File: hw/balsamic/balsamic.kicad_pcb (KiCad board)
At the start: 2 copper layers, 24 x 39 mm, 125 parts, among them J1 Conn_01x24, J2 USB_C_Receptacle, SW1 SW_Push, U1 ISP1807-LR-RS, U2 BMI160, U3 K210, U4 MAX77658AANX+, U5 GD25LQ, U6 MAX811LEUS-T, U7 SiP32431DR3, Y1 Crystal_GND24

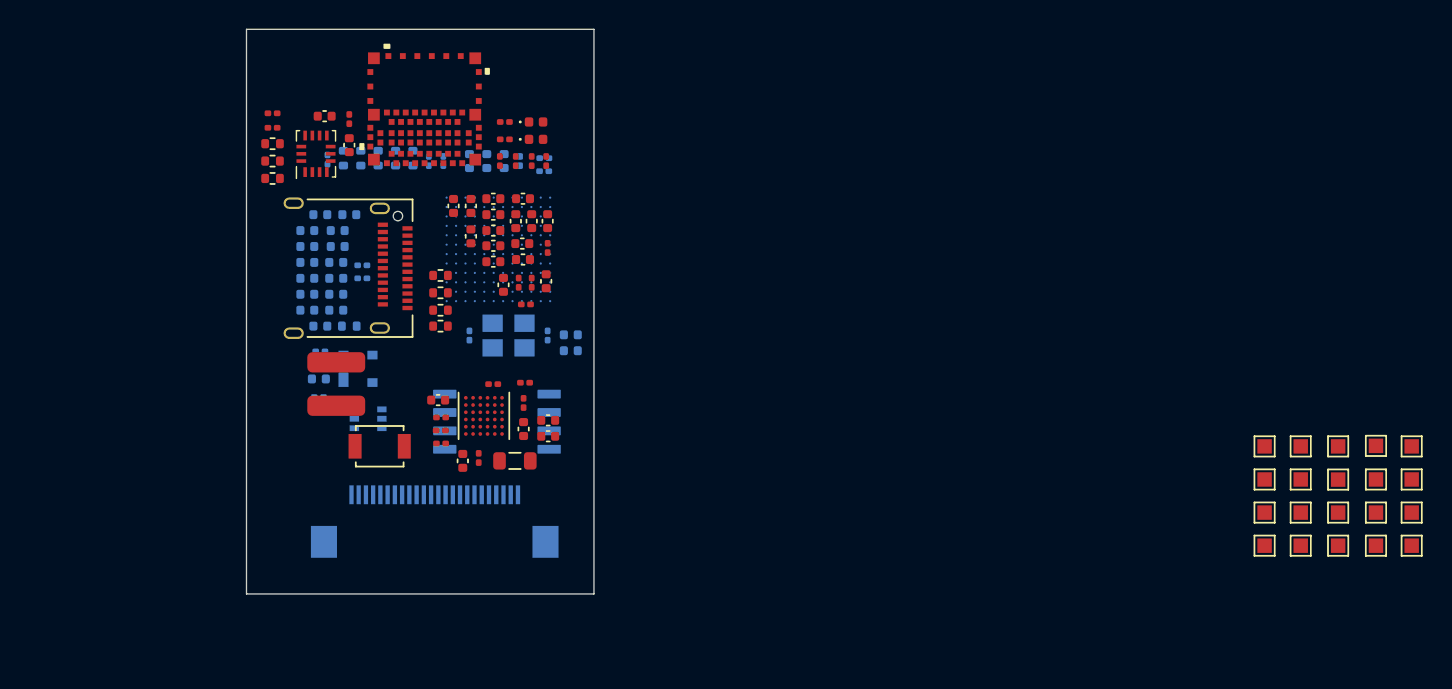
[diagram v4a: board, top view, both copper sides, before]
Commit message: Reduced spacing between ICs
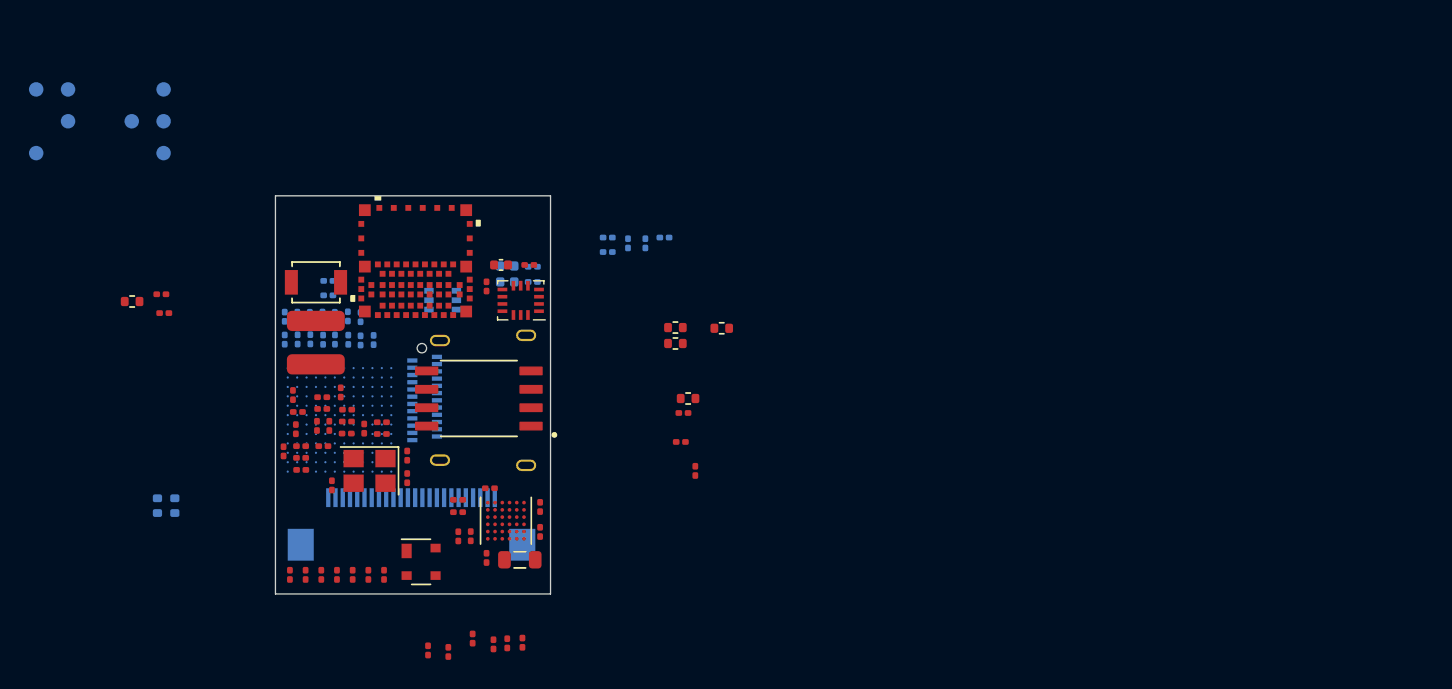
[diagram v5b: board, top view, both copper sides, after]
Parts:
- removed R21, R24, R29, R30, R31, R32: 0, Resistor_SMD:R_0402_1005Metric
- removed R4, R5: 5.1k, Resistor_SMD:R_0201_0603Metric
- removed TP1, TP10, TP11, TP12, TP13, TP2, TP3, TP4, TP6, TP7, TP8, TP9: TestPoint, TestPoint:TestPoint_Pad_1.0x1.0mm
- C1, C2, C50, R1, R15, R16, R25, R26, R27, R28, R35, U5, U6, Y1: moved to F.Cu
- C10, C11, C12, C14, C15, C16, C17, C18, C19, C20, C21, C22, C24, C25, C26, C27, C29, C30, C31, C32, C33, C35, C36, C37, C38, C4, C40, C41, C42, C43, C44, C45, C5, C51, C52, C6, C7, C8, C9: footprint Capacitor_SMD:C_0402_1005Metric -> Capacitor_SMD:C_0201_0603Metric
- C3, C47, C48, C49: footprint Capacitor_SMD:C_0402_1005Metric -> Capacitor_SMD:C_0201_0603Metric; moved to F.Cu
- D1, D2, J2, R22, R23, R33, R34: moved to B.Cu
- TP14, TP15, TP16, TP17, TP18, TP19, TP20, TP5: footprint TestPoint:TestPoint_Pad_1.0x1.0mm -> TestPoint:TestPoint_Pad_D1.0mm; moved to B.Cu
- moved TP17 98.2 mm to (45.5, 37.1), turned to 180 degrees
- moved TP15 97.6 mm to (45.5, 41.5), turned to 180 degrees
- moved TP5 93.1 mm to (47.7, 39.4), turned to 180 degrees
- moved TP19 91.1 mm to (47.7, 37.1), turned to 180 degrees
- moved TP18 81.7 mm to (54.3, 39.4), turned to 180 degrees
- moved TP16 81.4 mm to (52.1, 39.4), turned to 180 degrees
- moved TP14 80.7 mm to (54.3, 37.1), turned to 180 degrees
- moved TP20 80.0 mm to (54.3, 41.5), turned to 180 degrees
- moved R7 37.6 mm to (91.0, 63.5), turned to 90 degrees
- moved R8 35.1 mm to (90.2, 59.5)
- moved R16 32.4 mm to (64.1, 70.7), turned to 90 degrees
- moved R15 31.7 mm to (67.3, 70.7), turned to -90 degrees
- moved R1 31.2 mm to (90.0, 61.5), turned to 0 degrees
- moved C47 30.8 mm to (65.2, 70.7), turned to 90 degrees
- moved C50 30.1 mm to (69.5, 70.7), turned to -90 degrees
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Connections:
- J2 pad A5: Net-(J2-PadA5) -> nRF_UART_RX_DBUG
- J2 pad B10: Net-(J2-PadB10) -> Net-(J2-PadA10)
- J2 pad B11: Net-(J2-PadB11) -> Net-(J2-PadA11)
- J2 pad B2: Net-(J2-PadB2) -> Net-(J2-PadA2)
- J2 pad B3: Net-(J2-PadB3) -> Net-(J2-PadA3)
- J2 pad B5: Net-(J2-PadB5) -> nRF_UART_RX_DBUG
- J2 pad B6: Net-(J2-PadB6) -> Net-(J2-PadA6)
- J2 pad B7: Net-(J2-PadB7) -> Net-(J2-PadA7)
- R22 pad 1: Net-(J2-PadB7) -> Net-(J2-PadA7)
- R25 pad 1: Net-(J2-PadB10) -> Net-(J2-PadA10)
- R26 pad 1: Net-(J2-PadB11) -> Net-(J2-PadA11)
- U3 pad J11: JTAG_TMS -> unconnected-(U3-PadJ11)
- U3 pad J12: JTAG_TDO -> unconnected-(U3-PadJ12)
- U3 pad K11: JTAG_TCK -> unconnected-(U3-PadK11)
- U3 pad K12: JTAG_TDI -> unconnected-(U3-PadK12)
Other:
- board size 24 x 39 mm -> 19 x 27.5 mm

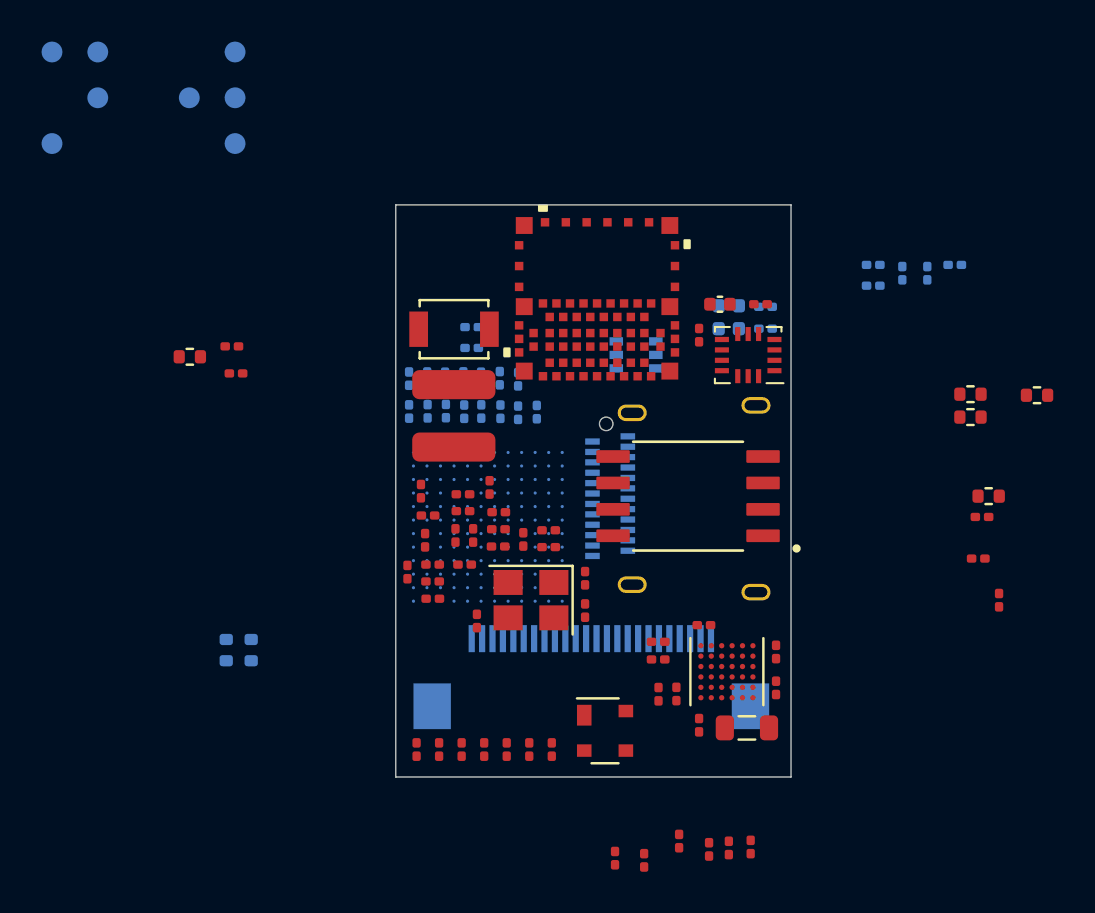
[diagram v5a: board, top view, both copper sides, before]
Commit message: began shrinking board w/out K210
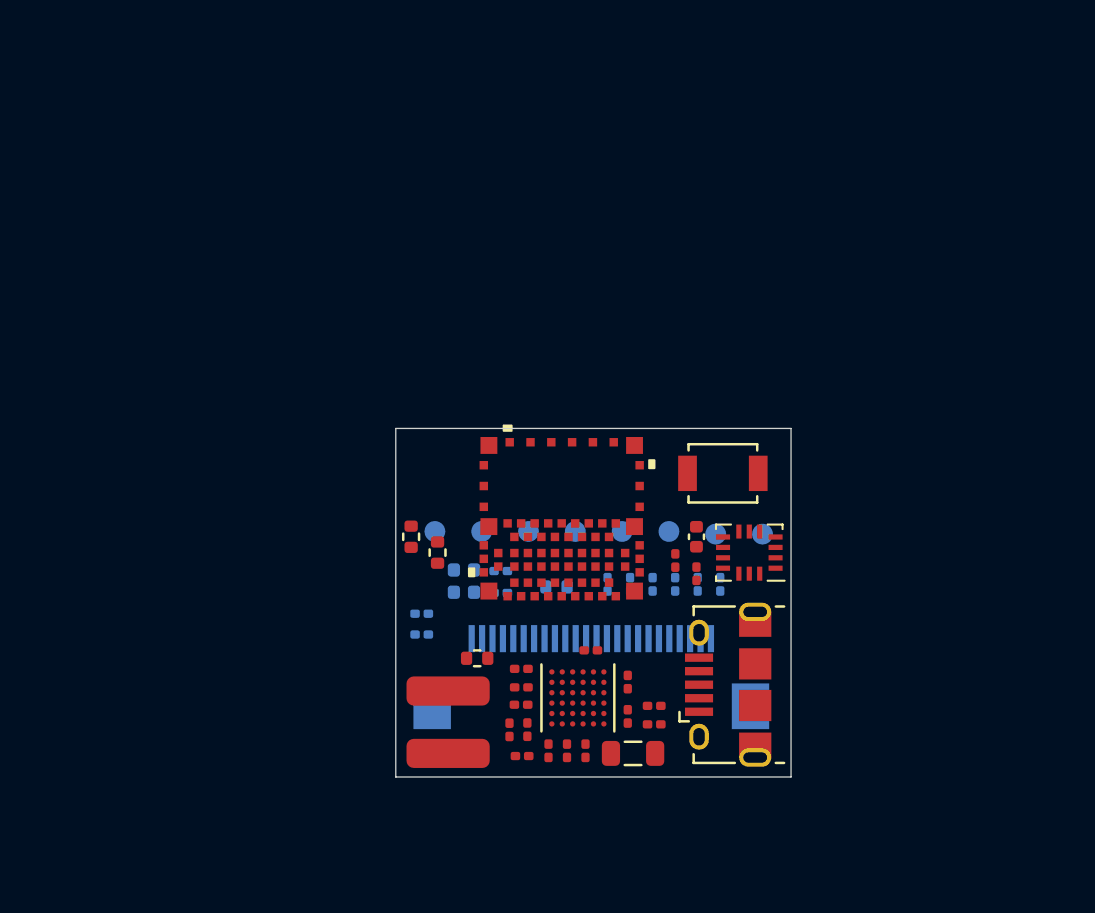
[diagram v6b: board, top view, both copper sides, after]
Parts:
- removed C1, C2: 4.7pF, Capacitor_SMD:C_0201_0603Metric
- removed C11, C5, C6, C8, C9: 4.7uF, Capacitor_SMD:C_0201_0603Metric
- removed C12, C15, C17, C18, C19, C20, C21, C22, C31, C33, C37, C38, C51: 10uF, Capacitor_SMD:C_0201_0603Metric
- removed C13, C24, C26, C29, C3, C32, C40, C42, C43, C44: 100nF, Capacitor_SMD:C_0201_0603Metric
- removed C14, C52: 1uF, Capacitor_SMD:C_0201_0603Metric
- removed C25, C27, C30, C35, C41: 100uF, Capacitor_SMD:C_0201_0603Metric
- removed FB1, FB2: FerriteBead_Small, Inductor_SMD:L_0201_0603Metric
- removed J2: USB_C_Receptacle, Connector_USB:USB_C_Receptacle_Amphenol_12401610E4-2A
- removed R13: 0, Resistor_SMD:R_0201_0603Metric
- removed R14: NO_STUFF, Resistor_SMD:R_0201_0603Metric
- removed R19: 100k, Resistor_SMD:R_0201_0603Metric
- removed R22, R23, R25, R26, R27, R28: 0, Resistor_SMD:R_0402_1005Metric
- removed R6: 1M, Resistor_SMD:R_0201_0603Metric
- removed R7: 1k, Resistor_SMD:R_0201_0603Metric
- removed R8: 2k, Resistor_SMD:R_0201_0603Metric
- removed U3: K210, footprints:Kendryte_K210
- removed U5: GD25LQ, footprints:SOIC127P790X216-8N
- removed U6: MAX811LEUS-T, Package_TO_SOT_SMD:SOT-143
- removed U7: SiP32431DR3, Package_TO_SOT_SMD:SOT-363_SC-70-6
- removed Y1: Crystal_GND24, Crystal:Crystal_SMD_3225-4Pin_3.2x2.5mm
- added J3: USB_B_Mini, Connector_USB:USB_Micro-B_Amphenol_10118194_Horizontal, F.Cu at (78.0, 67.6)
- C47, C48, C49, C50, R15, R16: moved to B.Cu
- R1: value 10k -> 0; footprint Resistor_SMD:R_0201_0603Metric -> Resistor_SMD:R_0402_1005Metric
- R2: footprint Resistor_SMD:R_0201_0603Metric -> Resistor_SMD:R_0402_1005Metric
- R3: footprint Resistor_SMD:R_0201_0603Metric -> Resistor_SMD:R_0402_1005Metric; moved to B.Cu
- moved TP14 34.3 mm to (79.6, 60.3)
- moved TP5 32.7 mm to (72.9, 60.2)
- moved TP19 32.5 mm to (70.6, 60.2)
- moved TP18 31.2 mm to (77.4, 60.3)
- moved TP16 31.1 mm to (75.1, 60.2)
- moved TP17 30.9 mm to (66.1, 60.2)
- moved TP15 29.5 mm to (68.4, 60.2)
- moved R1 27.3 mm to (62.7, 60.5), turned to 90 degrees
- moved TP20 21.0 mm to (63.9, 60.2)
- moved R35 20.0 mm to (65.9, 66.3), turned to 0 degrees
- moved R3 18.5 mm to (69.7, 62.9)
- moved R34 18.0 mm to (67.0, 62.1)
- moved R33 18.0 mm to (67.0, 63.1)
- moved D2 18.0 mm to (65.3, 62.0)
- moved D1 18.0 mm to (65.3, 63.1)
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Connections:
- R1 pad 1: SBB1_3.3V -> Net-(J3-Pad3)
- R1 pad 2: CH552_P1.1 -> nRF_SWDIO
- R2 pad 1: nRF_UART_RX -> Net-(J3-Pad2)
- R2 pad 2: Net-(R2-Pad2) -> nRF_SWDCLK
- R3 pad 1: Net-(R3-Pad1) -> nRF_UART_TX_DBUG
- R3 pad 2: nRF_UART_TX -> Net-(J3-Pad4)
- U1 pad 28: USB_D- -> nRF_SWDIO
- U1 pad 30: USB_D+ -> nRF_SWDCLK
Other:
- board size 19 x 27.5 mm -> 19 x 16.8 mm

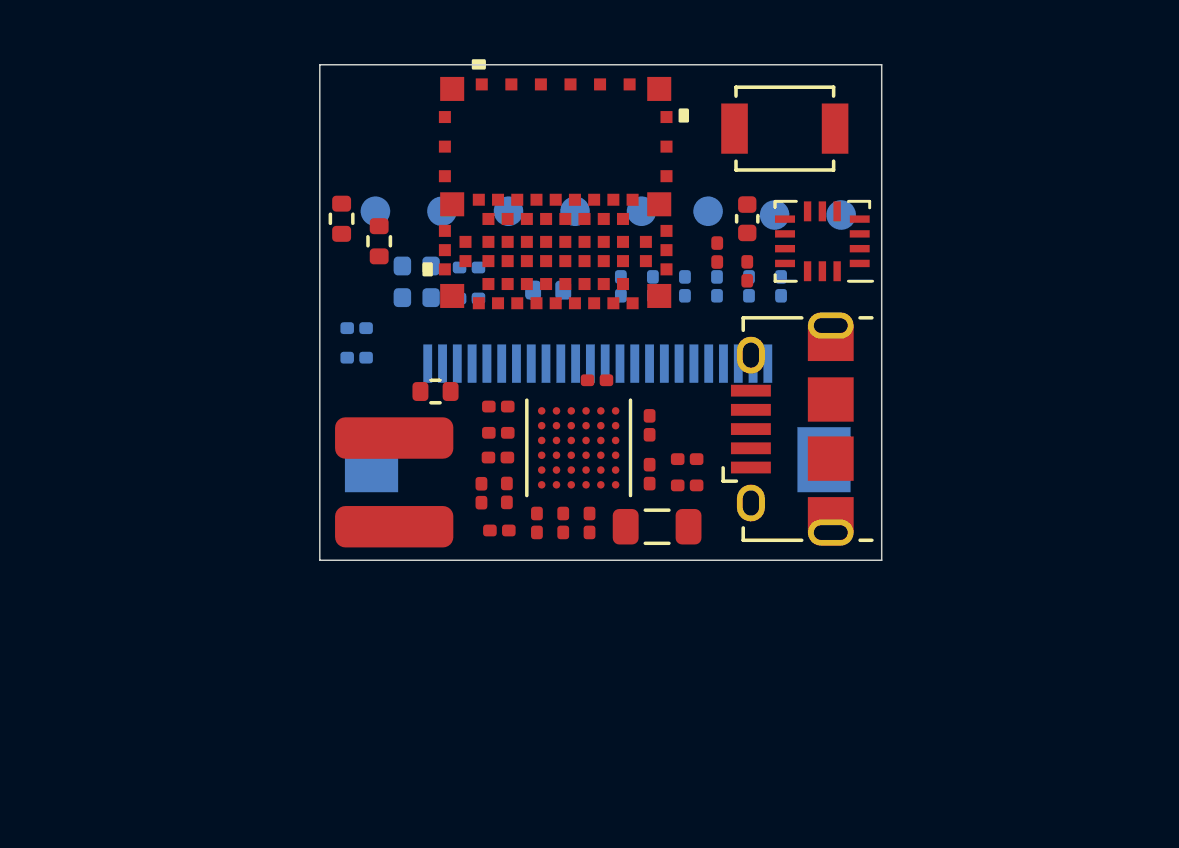
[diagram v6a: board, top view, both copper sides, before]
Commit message: switched to mezzanine camera connector
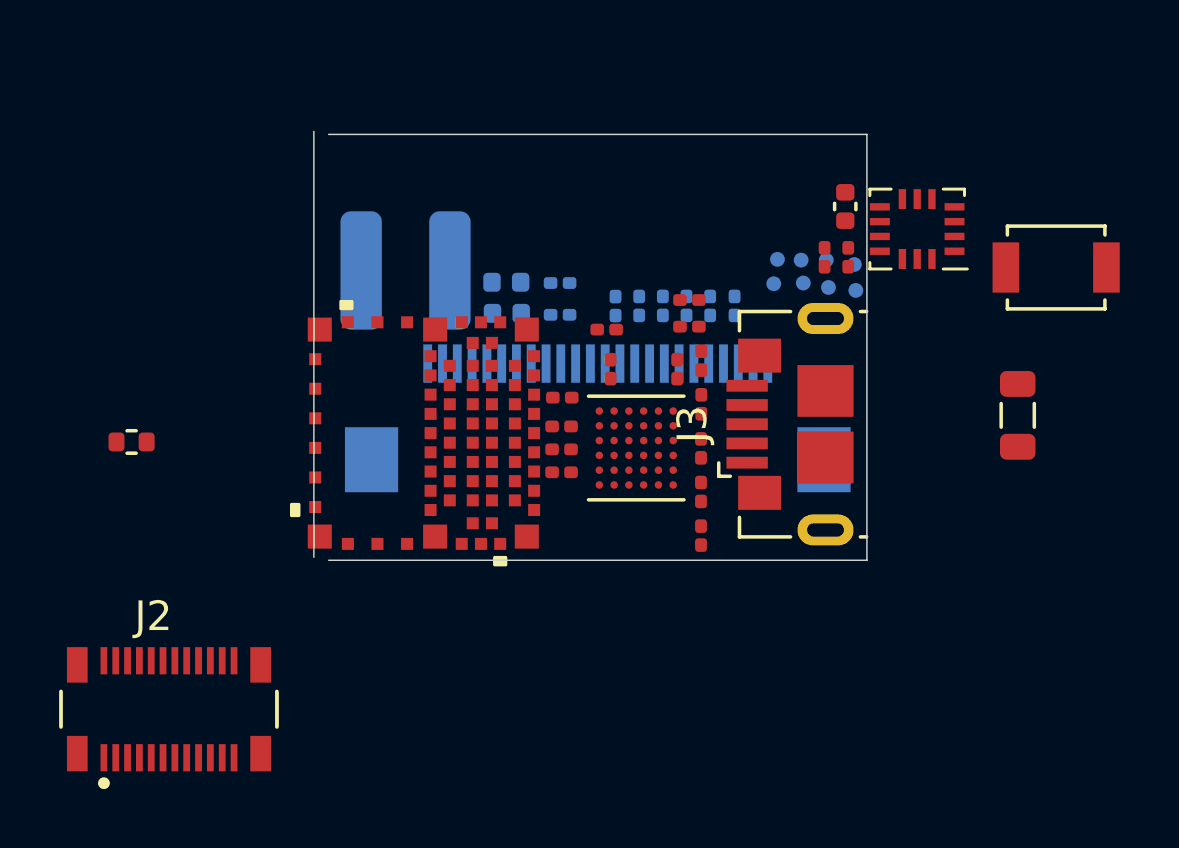
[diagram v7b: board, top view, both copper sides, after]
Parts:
- removed R1, R2, R3: 0, Resistor_SMD:R_0402_1005Metric
- removed R17, R18: 0, Resistor_SMD:R_0201_0603Metric
- added J2: AXT524124, footprints:PANASONIC_AXT524124, F.Cu at (56.9, 77.0)
- BT1: moved to B.Cu
- J3: footprint Connector_USB:USB_Micro-B_Amphenol_10118194_Horizontal -> Connector_USB:USB_Micro-B_GCT_USB3076-30-A
- TP14, TP15, TP16, TP17, TP18, TP19, TP20, TP5: footprint TestPoint:TestPoint_Pad_D1.0mm -> custom_testpoints:TestPoint_Pad_D0.5mm
- moved TP20 13.7 mm to (77.5, 61.8)
- moved L1 12.8 mm to (85.6, 67.1), turned to 90 degrees
- moved TP17 11.5 mm to (77.3, 62.6)
- moved R35 10.4 mm to (55.6, 68.0)
- moved SW1 10.3 mm to (86.9, 62.1)
- moved TP15 10.0 mm to (78.3, 61.9)
- moved U1 9.29 mm to (65.5, 67.7), turned to -90 degrees
- moved C16 9.01 mm to (74.5, 64.1), turned to 0 degrees
- moved C4 8.98 mm to (74.5, 63.2), turned to 0 degrees
- moved TP19 8.09 mm to (78.3, 62.6)
- moved R12 7.29 mm to (74.9, 65.2), turned to -90 degrees
- moved C53 6.95 mm to (71.7, 64.2), turned to 180 degrees
- moved C28 6.86 mm to (74.9, 66.7), turned to -90 degrees
- moved R11 6.76 mm to (74.1, 65.5), turned to -90 degrees
- moved C23 6.63 mm to (71.8, 65.5), turned to 90 degrees
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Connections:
- J1 pad 23: Net-(J1-Pad23) -> SBB1_3.3V
- J1 pad 24: Net-(J1-Pad24) -> PGND
- J3 pad 2: Net-(J3-Pad2) -> nRF_SWDCLK
- J3 pad 3: Net-(J3-Pad3) -> nRF_SWDIO
- J3 pad 4: Net-(J3-Pad4) -> nRF_UART_TX_DBUG
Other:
- board size 19 x 16.8 mm -> 18.7 x 14.5 mm
